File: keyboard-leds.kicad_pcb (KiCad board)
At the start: 2 copper layers, 87.7 x 51.5 mm, 53 parts, among them J1 USB_C_Receptacle_USB2.0_16P, J2 Conn_01x05, J4 Conn_01x03, J5 USB_C_Receptacle_USB2.0_16P, U1 RP2040, U2 W25Q128JVS, U3 XC6206PxxxMR-Regulator_Linear, U4 TFT_320x240, U5 TUSB320, U6 SN74AHCT1G125DBVR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

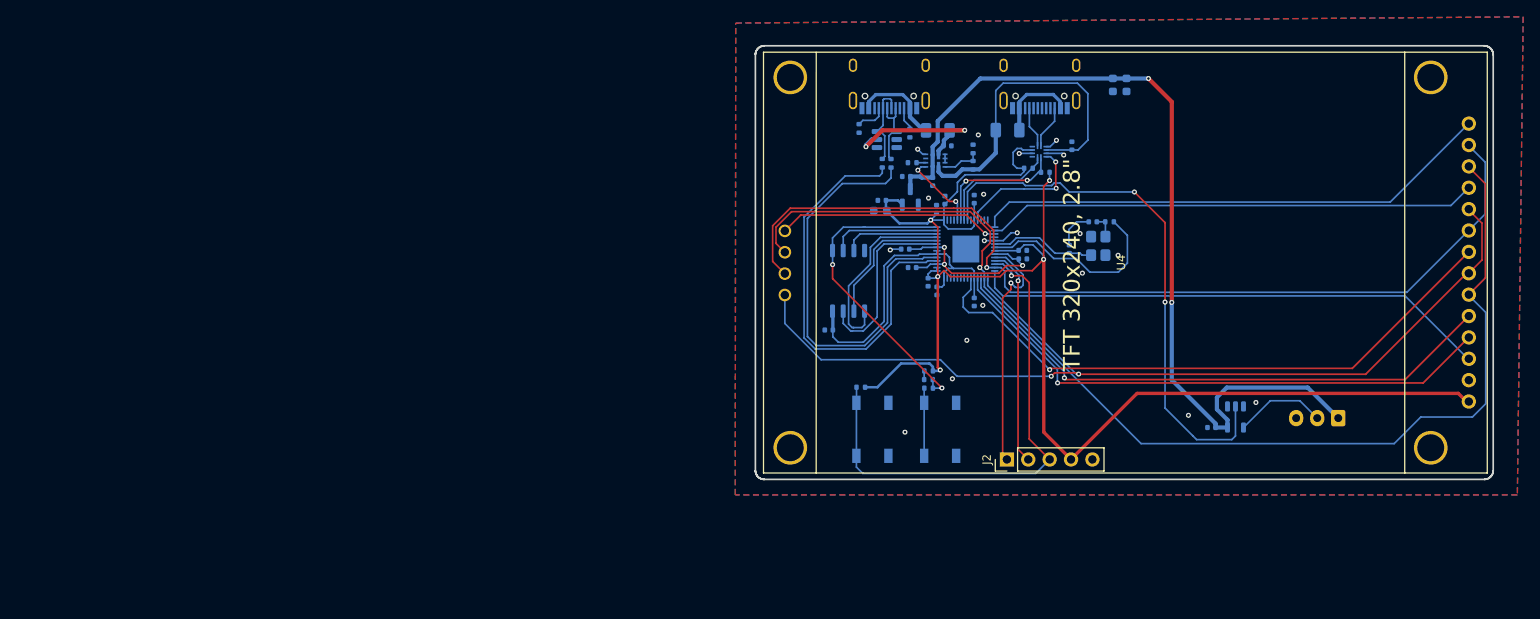
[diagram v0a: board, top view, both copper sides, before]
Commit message: Cleaned up footprints
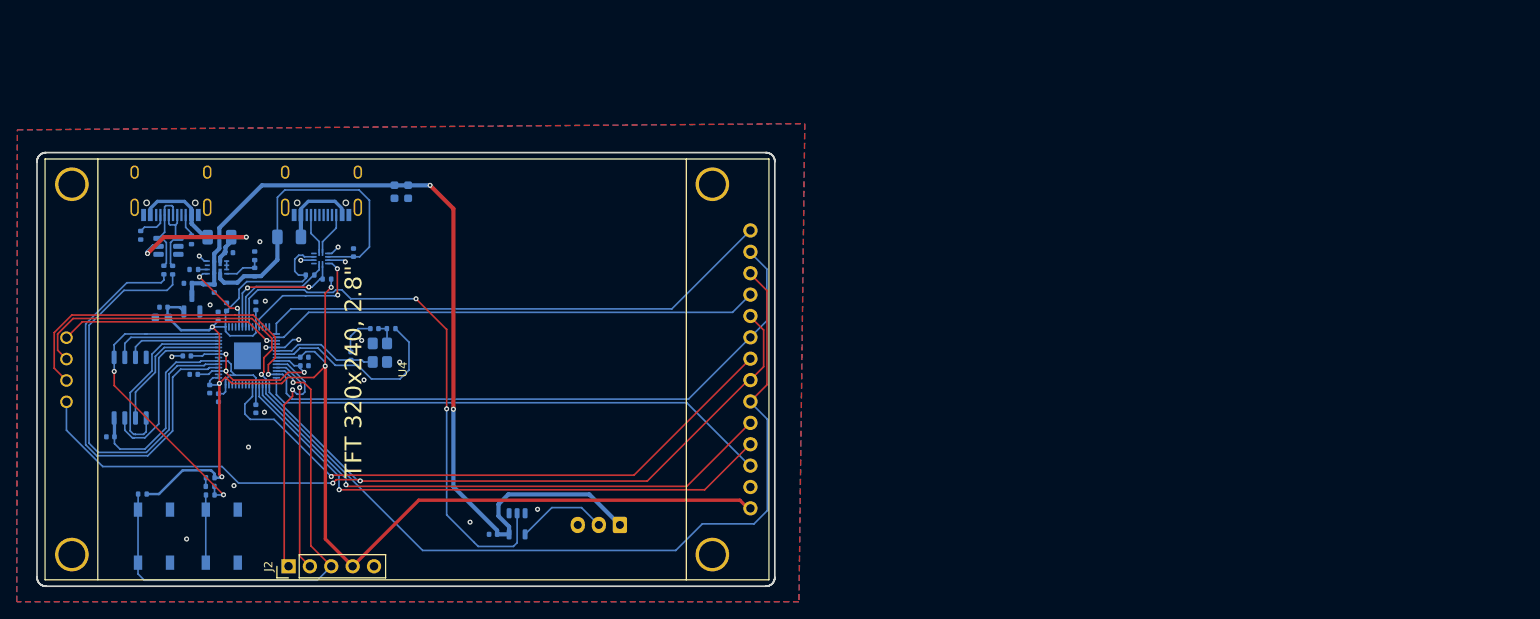
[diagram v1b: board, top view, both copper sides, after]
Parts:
- J1, J5: footprint PCM_marbastlib-various:USB_C_Receptacle_HRO_TYPE-C-31-M-12 -> ModHob:USB_C_Receptacle_HRO_TYPE-C-31-M-12
- moved C127 86.3 mm to (44.5, 41.7)
- moved F2 86.3 mm to (56.5, 36.2)
- moved C1 86.3 mm to (69.0, 30.9)
- moved C10 86.3 mm to (52.5, 56.6)
- moved C11 86.3 mm to (52.5, 44.4)
- moved C112 86.3 mm to (80.7, 71.6)
- moved C128 86.3 mm to (41.6, 44.6)
- moved C18 86.3 mm to (47.6, 42.3)
- moved C2 86.3 mm to (70.6, 30.9)
- moved C4 86.3 mm to (66.6, 47.1)
- moved C7 86.3 mm to (45.2, 52.6)
- moved C9 86.3 mm to (48.1, 55.3)
- moved J4 86.3 mm to (95.8, 70.4)
- moved R5 86.3 mm to (47.1, 65.9)
- moved U1 86.3 mm to (51.5, 50.4)
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
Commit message: Updates
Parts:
- added C19: 330u, Capacitor_Tantalum_SMD:CP_EIA-7343-31_Kemet-D, B.Cu at (75.1, 63.6)
- added C20: 330u, Capacitor_Tantalum_SMD:CP_EIA-7343-31_Kemet-D, B.Cu at (80.2, 63.6)
- C1: value 1000u -> 330u; footprint Capacitor_SMD:C_0603_1608Metric -> Capacitor_Tantalum_SMD:CP_EIA-7343-31_Kemet-D
- moved C1 36.6 mm to (85.3, 63.6), turned to 90 degrees
- moved C2 3.88 mm to (66.8, 30.1)
- moved C112 3.64 mm to (82.0, 75.0), turned to -90 degrees
- moved U6 3.02 mm to (84.3, 73.2)
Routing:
- net +5V: track 105.0 -> 128.6 mm
- net RGB3.3: track 65.1 -> 70.4 mm
- net LCD_MOSI: track 137.9 -> 140.6 mm
- net RGB5v: track 10.9 -> 13.1 mm
- net GND: vias 19 -> 20
